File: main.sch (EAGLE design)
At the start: 46 parts, among them IC1 MEGA8-AI, IC2 MCP73831, IC3 7805DT, Q2 32768k

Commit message: Schematics, PCB
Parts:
- removed D3: (no value), diode:DIODE-DO15-12
- added D4: (no value), diode:DIODE-D-7.5
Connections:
- net +3V3 renamed VDD
- net +12V: now also D4.C; no longer D3.C
- net DS1629_SCL: now also IC1.PC5(ADC5/SCL)
- net DS1629_SDA: now also IC1.PC4(ADC4/SDA)
- net N$19: now also IC1.PD4(XCK/T0)
- net N$20: now also IC1.PD0(RXD)
- net N$21: now also IC1.PD1(TXD)
- net N$22: now also IC1.PD2(INT0)
- net N$30: now also IC1.PD3(INT1)
- net N$35: now also IC1.PD5(T1)
- net N$36: now also IC1.PD6(AIN0)
- net N$5: now also D4.A; no longer D3.A
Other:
- moved on the sheet: R22
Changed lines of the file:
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@@
 <part name="P+5" library="supply1" deviceset="+12V" device=""/>
 <part name="GND8" library="supply1" deviceset="GND" device=""/>
-<part name="P+6" library="supply1" deviceset="+5V" device=""/>
-<part name="D3" library="diode" deviceset="DIODE-" device="DO15-12"/>
 <part name="R1" library="rcl" deviceset="R-EU_" device="M1206" value="200"/>
 <part name="D1" library="diode" deviceset="BZX84CSMD" device=""/>
@@
 <part name="R22" library="rcl" deviceset="R-EU_" device="R1206" value="10k"/>
 <part name="GND9" library="supply1" deviceset="GND" device=""/>
-<part name="P+7" library="supply1" deviceset="+5V" device=""/>
 <part name="S1" library="switch-omron" deviceset="10-XX" device="" value="MODE"/>
 <part name="IC1" library="atmel" deviceset="MEGA8" device="-AI"/>
+<part name="P+6" library="supply1" deviceset="+5V" device=""/>
+<part name="P+7" library="supply1" deviceset="+5V" device=""/>
+<part name="D4" library="diode" deviceset="DIODE-" device="D-7.5"/>
 </parts>
 <sheets>
@@
 <instance part="P+5" gate="1" x="218.44" y="208.28"/>
 <instance part="GND8" gate="1" x="218.44" y="165.1"/>
-<instance part="P+6" gate="1" x="129.54" y="162.56"/>
-<instance part="D3" gate="G$1" x="33.02" y="180.34"/>
 <instance part="R1" gate="G$1" x="38.1" y="170.18" rot="R90"/>
 <instance part="D1" gate="G$1" x="45.72" y="160.02" rot="R90"/>
 <instance part="T6" gate="G$1" x="45.72" y="177.8" rot="R90"/>
 <instance part="D2" gate="G$1" x="226.06" y="180.34" rot="R90"/>
-<instance part="R22" gate="G$1" x="236.22" y="157.48" rot="R90"/>
+<instance part="R22" gate="G$1" x="236.22" y="160.02" rot="R90"/>
 <instance part="GND9" gate="1" x="236.22" y="134.62"/>
-<instance part="P+7" gate="1" x="236.22" y="170.18"/>
 <instance part="S1" gate="1" x="236.22" y="144.78"/>
 <instance part="IC1" gate="G$1" x="167.64" y="127"/>
+<instance part="P+6" gate="1" x="129.54" y="162.56"/>
+<instance part="P+7" gate="1" x="236.22" y="170.18"/>
+<instance part="D4" gate="G$1" x="33.02" y="180.34"/>
 </instances>
 <busses>
@@
 </segment>
 <segment>
-<pinref part="P+6" gate="1" pin="+5V"/>
 <pinref part="C5" gate="G$1" pin="1"/>
 <wire x1="129.54" y1="111.76" x2="129.54" y2="114.3" width="0.1524" layer="91"/>
@@
 <wire x1="144.78" y1="142.24" x2="129.54" y2="142.24" width="0.1524" layer="91"/>
 <junction x="129.54" y="142.24"/>
-</segment>
-<segment>
+<pinref part="P+6" gate="1" pin="+5V"/>
+</segment>
+<segment>
+<pinref part="R22" gate="G$1" pin="2"/>
+<wire x1="236.22" y1="167.64" x2="236.22" y2="165.1" width="0.1524" layer="91"/>
 <pinref part="P+7" gate="1" pin="+5V"/>
-<pinref part="R22" gate="G$1" pin="2"/>
-<wire x1="236.22" y1="167.64" x2="236.22" y2="162.56" width="0.1524" layer="91"/>
 </segment>
 </net>
@@
 <net name="DS1629_SDA" class="0">
 <segment>
-<wire x1="193.04" y1="142.24" x2="198.12" y2="142.24" width="0.1524" layer="91"/>
-<label x="198.12" y="142.24" size="1.778" layer="95" xref="yes"/>
+<label x="203.2" y="142.24" size="1.778" layer="95" xref="yes"/>
+<pinref part="IC1" gate="G$1" pin="PC4(ADC4/SDA)"/>
+<wire x1="193.04" y1="142.24" x2="203.2" y2="142.24" width="0.1524" layer="91"/>
 </segment>
 <segment>
@@
 <net name="DS1629_SCL" class="0">
 <segment>
-<wire x1="193.04" y1="139.7" x2="198.12" y2="139.7" width="0.1524" layer="91"/>
-<label x="198.12" y="139.7" size="1.778" layer="95" xref="yes"/>
+<label x="203.2" y="139.7" size="1.778" layer="95" xref="yes"/>
+<pinref part="IC1" gate="G$1" pin="PC5(ADC5/SCL)"/>
+<wire x1="193.04" y1="139.7" x2="203.2" y2="139.7" width="0.1524" layer="91"/>
 </segment>
 <segment>
@@
 </segment>
 </net>
-<net name="+3V3" class="0">
+<net name="VDD" class="0">
 <segment>
 <pinref part="U$1" gate="G$1" pin="VDD"/>
@@
 <net name="N$20" class="0">
 <segment>
-<wire x1="215.9" y1="129.54" x2="193.04" y2="129.54" width="0.1524" layer="91"/>
 <pinref part="R13" gate="G$1" pin="1"/>
 <wire x1="215.9" y1="129.54" x2="215.9" y2="63.5" width="0.1524" layer="91"/>
 <wire x1="215.9" y1="63.5" x2="241.3" y2="63.5" width="0.1524" layer="91"/>
+<pinref part="IC1" gate="G$1" pin="PD0(RXD)"/>
+<wire x1="193.04" y1="129.54" x2="215.9" y2="129.54" width="0.1524" layer="91"/>
 </segment>
 </net>
 <net name="N$21" class="0">
 <segment>
-<wire x1="213.36" y1="127" x2="193.04" y2="127" width="0.1524" layer="91"/>
 <pinref part="R14" gate="G$1" pin="1"/>
 <wire x1="213.36" y1="127" x2="213.36" y2="58.42" width="0.1524" layer="91"/>
 <wire x1="213.36" y1="58.42" x2="241.3" y2="58.42" width="0.1524" layer="91"/>
+<pinref part="IC1" gate="G$1" pin="PD1(TXD)"/>
+<wire x1="193.04" y1="127" x2="213.36" y2="127" width="0.1524" layer="91"/>
 </segment>
 </net>
 <net name="N$22" class="0">
 <segment>
-<wire x1="210.82" y1="124.46" x2="193.04" y2="124.46" width="0.1524" layer="91"/>
 <pinref part="R15" gate="G$1" pin="1"/>
 <wire x1="210.82" y1="124.46" x2="210.82" y2="53.34" width="0.1524" layer="91"/>
 <wire x1="210.82" y1="53.34" x2="241.3" y2="53.34" width="0.1524" layer="91"/>
+<pinref part="IC1" gate="G$1" pin="PD2(INT0)"/>
+<wire x1="193.04" y1="124.46" x2="210.82" y2="124.46" width="0.1524" layer="91"/>
 </segment>
 </net>
 <net name="N$30" class="0">
 <segment>
-<wire x1="208.28" y1="121.92" x2="193.04" y2="121.92" width="0.1524" layer="91"/>
 <pinref part="R16" gate="G$1" pin="1"/>
 <wire x1="208.28" y1="121.92" x2="208.28" y2="48.26" width="0.1524" layer="91"/>
 <wire x1="208.28" y1="48.26" x2="241.3" y2="48.26" width="0.1524" layer="91"/>
+<pinref part="IC1" gate="G$1" pin="PD3(INT1)"/>
+<wire x1="193.04" y1="121.92" x2="208.28" y2="121.92" width="0.1524" layer="91"/>
 </segment>
 </net>
@@
 <net name="N$19" class="0">
 <segment>
-<wire x1="205.74" y1="119.38" x2="193.04" y2="119.38" width="0.1524" layer="91"/>
 <pinref part="R17" gate="G$1" pin="1"/>
 <wire x1="205.74" y1="119.38" x2="205.74" y2="43.18" width="0.1524" layer="91"/>
 <wire x1="205.74" y1="43.18" x2="241.3" y2="43.18" width="0.1524" layer="91"/>
+<pinref part="IC1" gate="G$1" pin="PD4(XCK/T0)"/>
+<wire x1="193.04" y1="119.38" x2="205.74" y2="119.38" width="0.1524" layer="91"/>
 </segment>
 </net>
 <net name="N$35" class="0">
 <segment>
-<wire x1="203.2" y1="116.84" x2="193.04" y2="116.84" width="0.1524" layer="91"/>
 <pinref part="R18" gate="G$1" pin="1"/>
 <wire x1="203.2" y1="116.84" x2="203.2" y2="38.1" width="0.1524" layer="91"/>
 <wire x1="203.2" y1="38.1" x2="241.3" y2="38.1" width="0.1524" layer="91"/>
+<pinref part="IC1" gate="G$1" pin="PD5(T1)"/>
+<wire x1="193.04" y1="116.84" x2="203.2" y2="116.84" width="0.1524" layer="91"/>
 </segment>
 </net>
 <net name="N$36" class="0">
 <segment>
-<wire x1="200.66" y1="114.3" x2="193.04" y2="114.3" width="0.1524" layer="91"/>
 <pinref part="R19" gate="G$1" pin="1"/>
 <wire x1="200.66" y1="114.3" x2="200.66" y2="33.02" width="0.1524" layer="91"/>
 <wire x1="200.66" y1="33.02" x2="241.3" y2="33.02" width="0.1524" layer="91"/>
+<pinref part="IC1" gate="G$1" pin="PD6(AIN0)"/>
+<wire x1="193.04" y1="114.3" x2="200.66" y2="114.3" width="0.1524" layer="91"/>
 </segment>
 </net>
@@
 </segment>
 <segment>
-<pinref part="D3" gate="G$1" pin="C"/>
-<wire x1="35.56" y1="180.34" x2="38.1" y2="180.34" width="0.1524" layer="91"/>
 <pinref part="T6" gate="G$1" pin="C"/>
 <pinref part="R1" gate="G$1" pin="2"/>
@@
 <pinref part="P+4" gate="1" pin="+12V"/>
 <wire x1="38.1" y1="193.04" x2="38.1" y2="180.34" width="0.1524" layer="91"/>
+<pinref part="D4" gate="G$1" pin="C"/>
+<wire x1="35.56" y1="180.34" x2="38.1" y2="180.34" width="0.1524" layer="91"/>
 </segment>
 </net>
@@
 <wire x1="218.44" y1="185.42" x2="218.44" y2="187.96" width="0.1524" layer="91"/>
 <wire x1="218.44" y1="187.96" x2="218.44" y2="190.5" width="0.1524" layer="91"/>
-<wire x1="193.04" y1="134.62" x2="198.12" y2="134.62" width="0.1524" layer="91"/>
-<wire x1="198.12" y1="134.62" x2="198.12" y2="187.96" width="0.1524" layer="91"/>
-<wire x1="198.12" y1="187.96" x2="218.44" y2="187.96" width="0.1524" layer="91"/>
+<wire x1="193.04" y1="134.62" x2="208.28" y2="134.62" width="0.1524" layer="91"/>
+<wire x1="208.28" y1="134.62" x2="208.28" y2="187.96" width="0.1524" layer="91"/>
+<wire x1="208.28" y1="187.96" x2="218.44" y2="187.96" width="0.1524" layer="91"/>
 <junction x="218.44" y="187.96"/>
 <wire x1="218.44" y1="187.96" x2="226.06" y2="187.96" width="0.1524" layer="91"/>
@@
 </segment>
 </net>
-<net name="N$5" class="0">
-<segment>
-<pinref part="JP1" gate="G$1" pin="1"/>
-<wire x1="20.32" y1="180.34" x2="30.48" y2="180.34" width="0.1524" layer="91"/>
-<pinref part="D3" gate="G$1" pin="A"/>
-</segment>
-</net>
 <net name="N$6" class="0">
 <segment>
@@
 <net name="N$38" class="0">
 <segment>
-<pinref part="R22" gate="G$1" pin="1"/>
-<pinref part="S1" gate="1" pin="S"/>
-<wire x1="223.52" y1="152.4" x2="236.22" y2="152.4" width="0.1524" layer="91"/>
-<wire x1="236.22" y1="152.4" x2="236.22" y2="149.86" width="0.1524" layer="91"/>
 <pinref part="IC1" gate="G$1" pin="PB0(ICP)"/>
 <wire x1="223.52" y1="152.4" x2="223.52" y2="106.68" width="0.1524" layer="91"/>
 <wire x1="223.52" y1="106.68" x2="193.04" y2="106.68" width="0.1524" layer="91"/>
+<pinref part="S1" gate="1" pin="S"/>
+<pinref part="R22" gate="G$1" pin="1"/>
+<wire x1="236.22" y1="154.94" x2="236.22" y2="152.4" width="0.1524" layer="91"/>
+<wire x1="236.22" y1="152.4" x2="236.22" y2="149.86" width="0.1524" layer="91"/>
+<wire x1="223.52" y1="152.4" x2="236.22" y2="152.4" width="0.1524" layer="91"/>
+<junction x="236.22" y="152.4"/>
+</segment>
+</net>
+<net name="N$5" class="0">
+<segment>
+<pinref part="JP1" gate="G$1" pin="1"/>
+<pinref part="D4" gate="G$1" pin="A"/>
+<wire x1="20.32" y1="180.34" x2="30.48" y2="180.34" width="0.1524" layer="91"/>
 </segment>
 </net>
@@
 </sheet>
 </sheets>
-<errors>
-</errors>
 </schematic>
 </drawing>

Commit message: Schematics
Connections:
- net N$38: now also IC1.ADC6; no longer IC1.PB0(ICP)
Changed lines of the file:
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@@
 <net name="N$38" class="0">
 <segment>
-<pinref part="IC1" gate="G$1" pin="PB0(ICP)"/>
-<wire x1="223.52" y1="152.4" x2="223.52" y2="106.68" width="0.1524" layer="91"/>
-<wire x1="223.52" y1="106.68" x2="193.04" y2="106.68" width="0.1524" layer="91"/>
 <pinref part="S1" gate="1" pin="S"/>
 <pinref part="R22" gate="G$1" pin="1"/>
@@
 <wire x1="223.52" y1="152.4" x2="236.22" y2="152.4" width="0.1524" layer="91"/>
 <junction x="236.22" y="152.4"/>
+<pinref part="IC1" gate="G$1" pin="ADC6"/>
+<wire x1="223.52" y1="152.4" x2="223.52" y2="137.16" width="0.1524" layer="91"/>
+<wire x1="223.52" y1="137.16" x2="193.04" y2="137.16" width="0.1524" layer="91"/>
 </segment>
 </net>

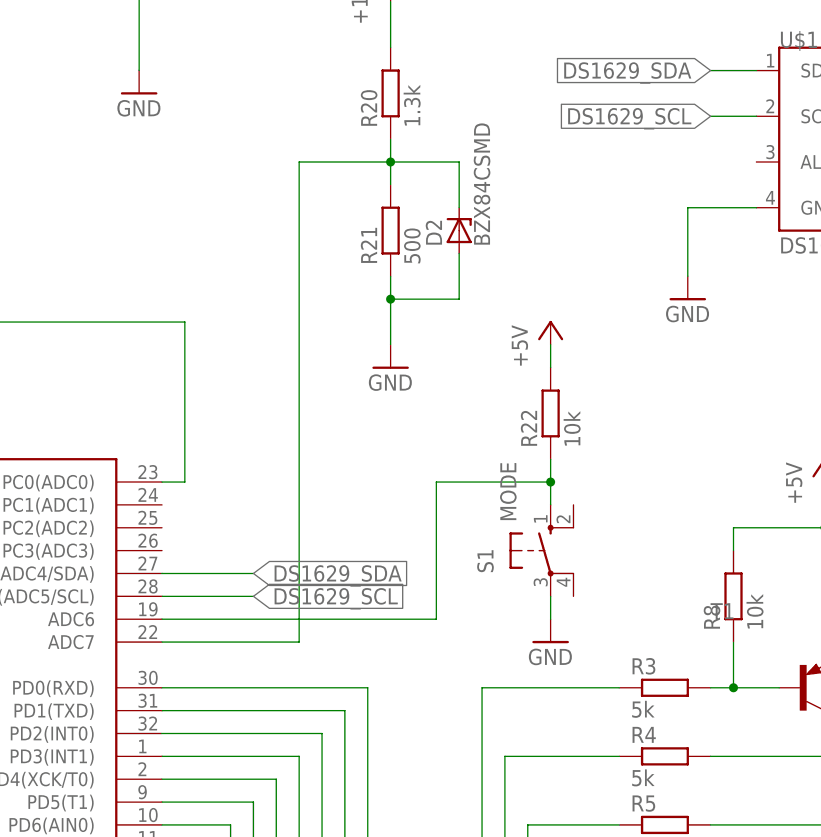
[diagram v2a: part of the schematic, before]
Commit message: Button noise rejection
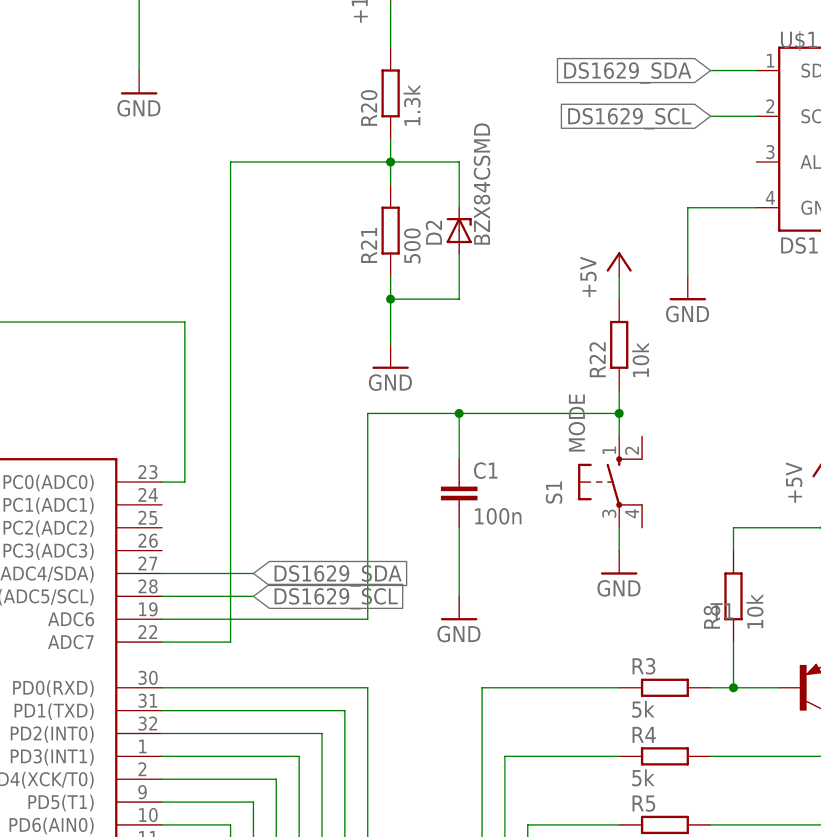
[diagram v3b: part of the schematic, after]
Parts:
- added C1: 100n, rcl:C-EUC1206
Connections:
- net GND: now also C1.2
- net N$38: now also C1.1
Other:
- moved on the sheet: R22, S1
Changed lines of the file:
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@@
 <part name="P+7" library="supply1" deviceset="+5V" device=""/>
 <part name="D4" library="diode" deviceset="DIODE-" device="D-7.5"/>
+<part name="C1" library="rcl" deviceset="C-EU" device="C1206" value="100n"/>
+<part name="GND10" library="supply1" deviceset="GND" device=""/>
 </parts>
 <sheets>
@@
 <instance part="T6" gate="G$1" x="45.72" y="177.8" rot="R90"/>
 <instance part="D2" gate="G$1" x="226.06" y="180.34" rot="R90"/>
-<instance part="R22" gate="G$1" x="236.22" y="160.02" rot="R90"/>
-<instance part="GND9" gate="1" x="236.22" y="134.62"/>
-<instance part="S1" gate="1" x="236.22" y="144.78"/>
+<instance part="R22" gate="G$1" x="243.84" y="167.64" rot="R90"/>
+<instance part="GND9" gate="1" x="243.84" y="142.24"/>
+<instance part="S1" gate="1" x="243.84" y="152.4"/>
 <instance part="IC1" gate="G$1" x="167.64" y="127"/>
 <instance part="P+6" gate="1" x="129.54" y="162.56"/>
-<instance part="P+7" gate="1" x="236.22" y="170.18"/>
+<instance part="P+7" gate="1" x="243.84" y="177.8"/>
 <instance part="D4" gate="G$1" x="33.02" y="180.34"/>
+<instance part="C1" gate="G$1" x="226.06" y="152.4"/>
+<instance part="GND10" gate="1" x="226.06" y="137.16"/>
 </instances>
 <busses>
@@
 <segment>
 <pinref part="GND9" gate="1" pin="GND"/>
-<wire x1="236.22" y1="139.7" x2="236.22" y2="137.16" width="0.1524" layer="91"/>
+<wire x1="243.84" y1="147.32" x2="243.84" y2="144.78" width="0.1524" layer="91"/>
 <pinref part="S1" gate="1" pin="P"/>
+</segment>
+<segment>
+<pinref part="GND10" gate="1" pin="GND"/>
+<pinref part="C1" gate="G$1" pin="2"/>
+<wire x1="226.06" y1="139.7" x2="226.06" y2="147.32" width="0.1524" layer="91"/>
 </segment>
 </net>
@@
 <segment>
 <pinref part="R22" gate="G$1" pin="2"/>
-<wire x1="236.22" y1="167.64" x2="236.22" y2="165.1" width="0.1524" layer="91"/>
+<wire x1="243.84" y1="175.26" x2="243.84" y2="172.72" width="0.1524" layer="91"/>
 <pinref part="P+7" gate="1" pin="+5V"/>
 </segment>
@@
 <wire x1="218.44" y1="185.42" x2="218.44" y2="187.96" width="0.1524" layer="91"/>
 <wire x1="218.44" y1="187.96" x2="218.44" y2="190.5" width="0.1524" layer="91"/>
-<wire x1="193.04" y1="134.62" x2="208.28" y2="134.62" width="0.1524" layer="91"/>
-<wire x1="208.28" y1="134.62" x2="208.28" y2="187.96" width="0.1524" layer="91"/>
-<wire x1="208.28" y1="187.96" x2="218.44" y2="187.96" width="0.1524" layer="91"/>
+<wire x1="193.04" y1="134.62" x2="200.66" y2="134.62" width="0.1524" layer="91"/>
+<wire x1="200.66" y1="134.62" x2="200.66" y2="187.96" width="0.1524" layer="91"/>
+<wire x1="200.66" y1="187.96" x2="218.44" y2="187.96" width="0.1524" layer="91"/>
 <junction x="218.44" y="187.96"/>
 <wire x1="218.44" y1="187.96" x2="226.06" y2="187.96" width="0.1524" layer="91"/>
@@
 <pinref part="S1" gate="1" pin="S"/>
 <pinref part="R22" gate="G$1" pin="1"/>
-<wire x1="236.22" y1="154.94" x2="236.22" y2="152.4" width="0.1524" layer="91"/>
-<wire x1="236.22" y1="152.4" x2="236.22" y2="149.86" width="0.1524" layer="91"/>
-<wire x1="223.52" y1="152.4" x2="236.22" y2="152.4" width="0.1524" layer="91"/>
-<junction x="236.22" y="152.4"/>
+<wire x1="243.84" y1="162.56" x2="243.84" y2="160.02" width="0.1524" layer="91"/>
+<wire x1="243.84" y1="160.02" x2="243.84" y2="157.48" width="0.1524" layer="91"/>
+<wire x1="215.9" y1="160.02" x2="226.06" y2="160.02" width="0.1524" layer="91"/>
+<junction x="243.84" y="160.02"/>
 <pinref part="IC1" gate="G$1" pin="ADC6"/>
-<wire x1="223.52" y1="152.4" x2="223.52" y2="137.16" width="0.1524" layer="91"/>
-<wire x1="223.52" y1="137.16" x2="193.04" y2="137.16" width="0.1524" layer="91"/>
-</segment>
-</net>
+<wire x1="226.06" y1="160.02" x2="243.84" y2="160.02" width="0.1524" layer="91"/>
+<wire x1="215.9" y1="160.02" x2="215.9" y2="137.16" width="0.1524" layer="91"/>
+<wire x1="215.9" y1="137.16" x2="193.04" y2="137.16" width="0.1524" layer="91"/>
+<pinref part="C1" gate="G$1" pin="1"/>
+<wire x1="226.06" y1="160.02" x2="226.06" y2="154.94" width="0.1524" layer="91"/>
+<junction x="226.06" y="160.02"/>
+</segment>
+</net>

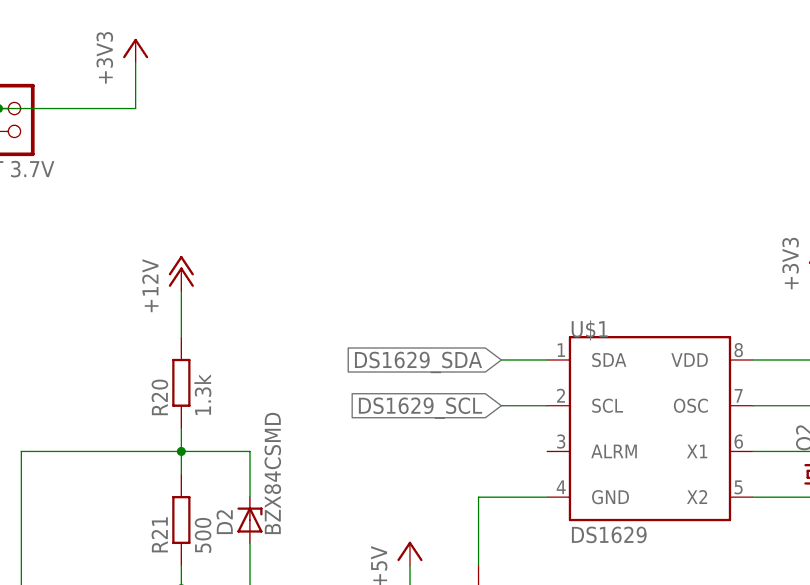
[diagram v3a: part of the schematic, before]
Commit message: Pull-up resistors on TWI bus
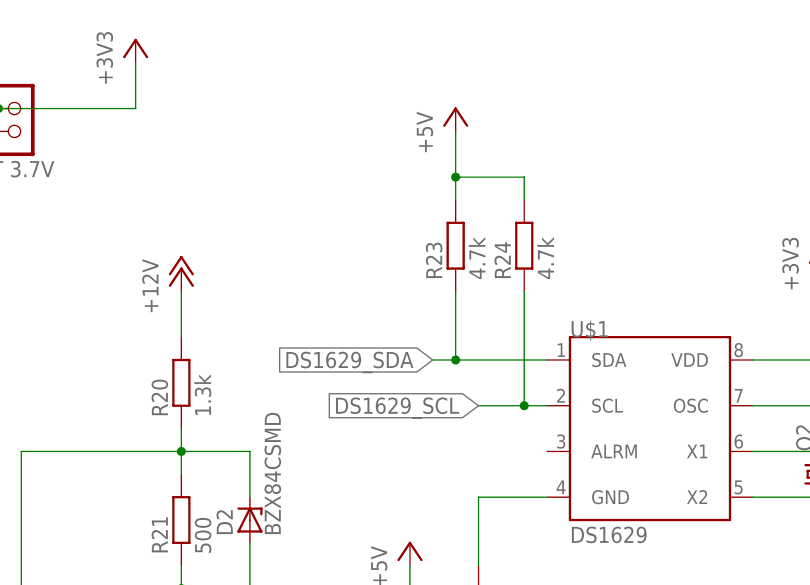
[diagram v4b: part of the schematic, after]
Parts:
- added R23, R24: 4.7k, rcl:R-EU_R1206
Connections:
- net +5V: now also R23.2, R24.2
- net DS1629_SCL: now also R24.1
- net DS1629_SDA: now also R23.1
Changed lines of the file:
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@@
 <part name="C1" library="rcl" deviceset="C-EU" device="C1206" value="100n"/>
 <part name="GND10" library="supply1" deviceset="GND" device=""/>
+<part name="P+8" library="supply1" deviceset="+5V" device=""/>
+<part name="R23" library="rcl" deviceset="R-EU_" device="R1206" value="4.7k"/>
+<part name="R24" library="rcl" deviceset="R-EU_" device="R1206" value="4.7k"/>
 </parts>
 <sheets>
@@
 <instance part="C1" gate="G$1" x="226.06" y="152.4"/>
 <instance part="GND10" gate="1" x="226.06" y="137.16"/>
+<instance part="P+8" gate="1" x="248.92" y="226.06"/>
+<instance part="R23" gate="G$1" x="248.92" y="210.82" rot="R90"/>
+<instance part="R24" gate="G$1" x="256.54" y="210.82" rot="R90"/>
 </instances>
 <busses>
@@
 <pinref part="P+7" gate="1" pin="+5V"/>
 </segment>
+<segment>
+<pinref part="P+8" gate="1" pin="+5V"/>
+<pinref part="R23" gate="G$1" pin="2"/>
+<wire x1="248.92" y1="223.52" x2="248.92" y2="218.44" width="0.1524" layer="91"/>
+<pinref part="R24" gate="G$1" pin="2"/>
+<wire x1="248.92" y1="218.44" x2="248.92" y2="215.9" width="0.1524" layer="91"/>
+<wire x1="248.92" y1="218.44" x2="256.54" y2="218.44" width="0.1524" layer="91"/>
+<wire x1="256.54" y1="218.44" x2="256.54" y2="215.9" width="0.1524" layer="91"/>
+<junction x="248.92" y="218.44"/>
+</segment>
 </net>
 <net name="N$8" class="0">
@@
 <segment>
 <pinref part="U$1" gate="G$1" pin="SDA"/>
-<wire x1="259.08" y1="198.12" x2="254" y2="198.12" width="0.1524" layer="91"/>
-<label x="254" y="198.12" size="1.778" layer="95" rot="R180" xref="yes"/>
+<wire x1="259.08" y1="198.12" x2="248.92" y2="198.12" width="0.1524" layer="91"/>
+<label x="246.38" y="198.12" size="1.778" layer="95" rot="R180" xref="yes"/>
+<pinref part="R23" gate="G$1" pin="1"/>
+<wire x1="248.92" y1="198.12" x2="246.38" y2="198.12" width="0.1524" layer="91"/>
+<wire x1="248.92" y1="205.74" x2="248.92" y2="198.12" width="0.1524" layer="91"/>
+<junction x="248.92" y="198.12"/>
 </segment>
 </net>
@@
 <segment>
 <pinref part="U$1" gate="G$1" pin="SCL"/>
-<wire x1="259.08" y1="193.04" x2="254" y2="193.04" width="0.1524" layer="91"/>
-<label x="254" y="193.04" size="1.778" layer="95" rot="R180" xref="yes"/>
-</segment>
-</net>
+<wire x1="259.08" y1="193.04" x2="256.54" y2="193.04" width="0.1524" layer="91"/>
+<label x="251.46" y="193.04" size="1.778" layer="95" rot="R180" xref="yes"/>
+<pinref part="R24" gate="G$1" pin="1"/>
+<wire x1="256.54" y1="193.04" x2="251.46" y2="193.04" width="0.1524" layer="91"/>
+<wire x1="256.54" y1="205.74" x2="256.54" y2="193.04" width="0.1524" layer="91"/>
+<junction x="256.54" y="193.04"/>
+</segment>
+</net>
